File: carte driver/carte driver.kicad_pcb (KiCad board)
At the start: 2 copper layers, 120 x 50 mm, 76 parts, among them J1 UART CP, J10 STEPPER 4, J11 STEPPER 3, J2 Conn_01x03, J3 UART BONUS, J4 Conn_01x02, J6 STEPPER G, J7 STEPPER D, J8 STEPPER 1, J9 STEPPER 2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

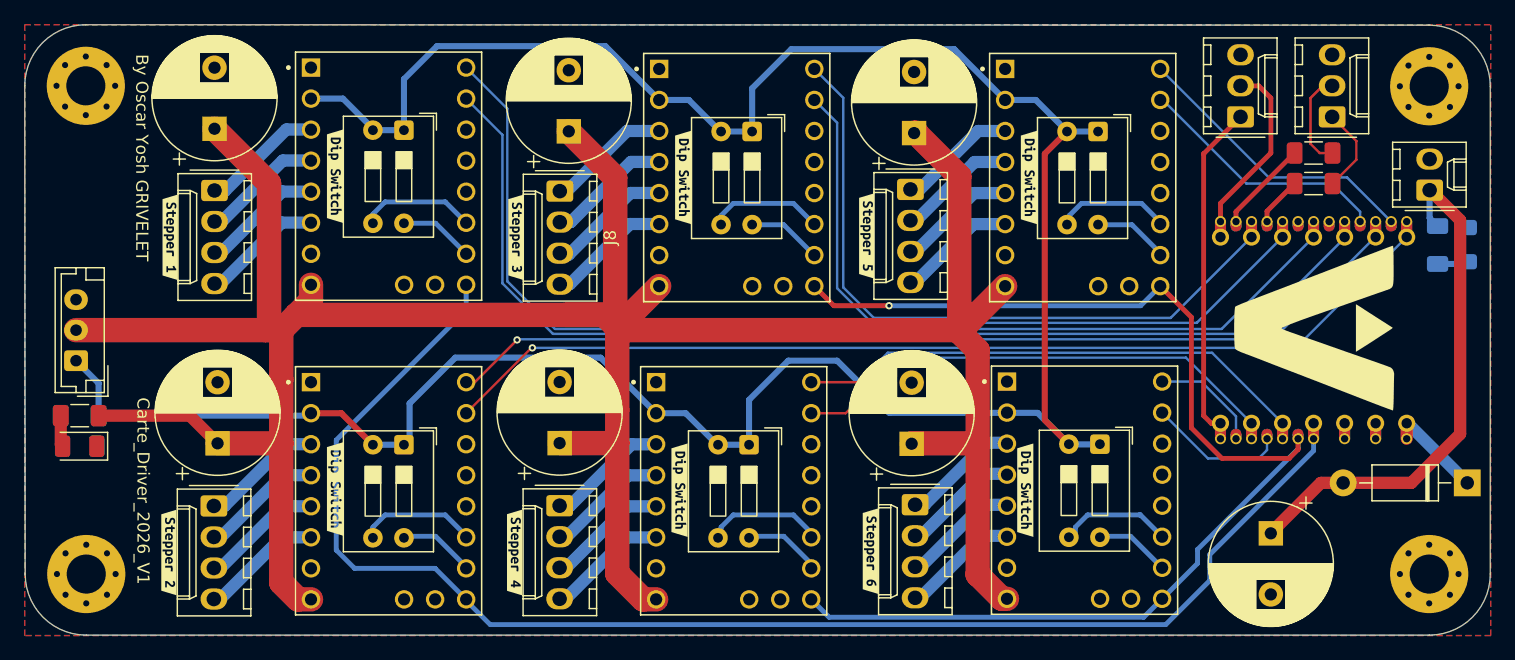
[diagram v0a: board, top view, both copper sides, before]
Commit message: changes power input and draw modif
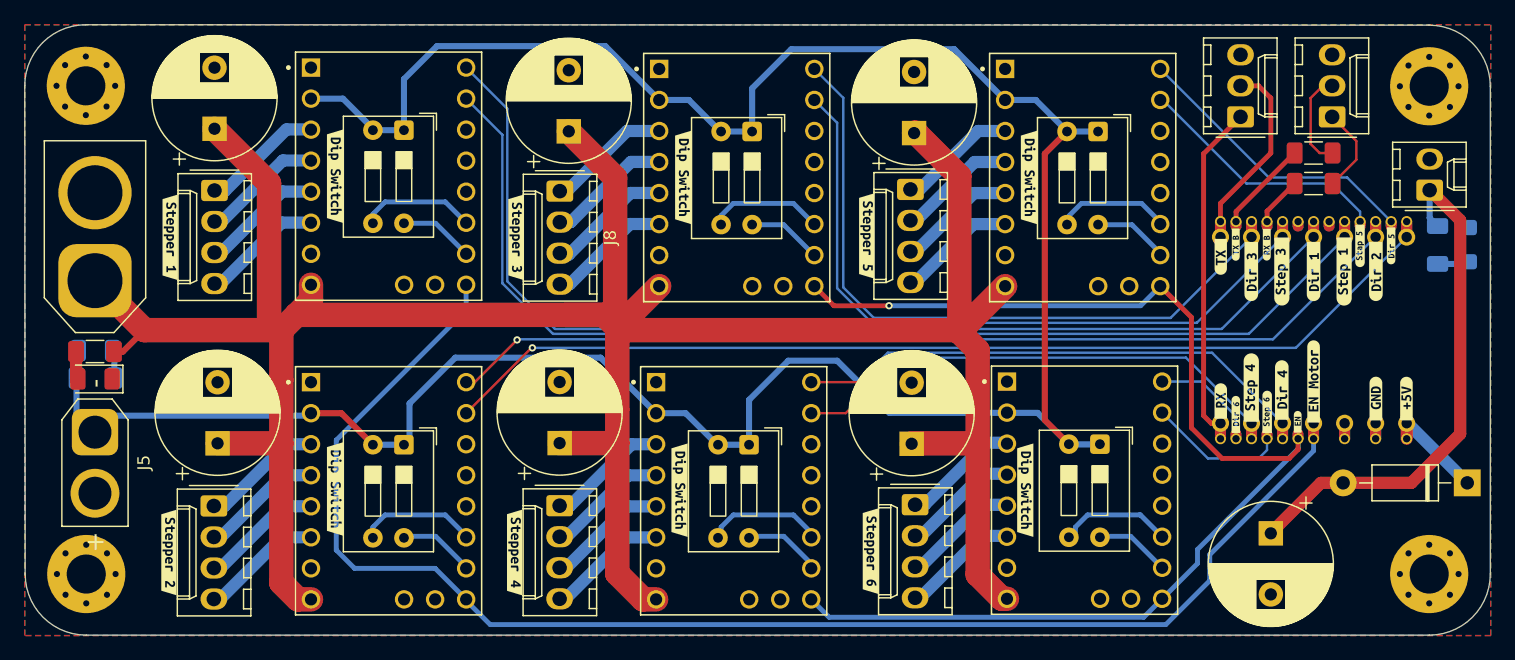
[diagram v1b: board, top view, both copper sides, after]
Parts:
- removed the G*** at (130.7, 150.0)
- removed J2: Conn_01x03, Connector_JST:JST_EH_B3B-EH-A_1x03_P2.50mm_Vertical
- removed the kibuzzard-68F7E6E6 at (126.7, 143.2)
- added J12: Conn_01x02, Connector_AMASS:AMASS_XT60-F_1x02_P7.20mm_Vertical, F.Cu at (30.8, 145.9)
- added J5: Conn_01x02, Connector_AMASS:AMASS_XT30U-F_1x02_P5.0mm_Vertical, F.Cu at (30.8, 158.3)
- added kibuzzard-690B42CF: G***, kibuzzard-690B42CF, F.Cu at (126.7, 143.0)
- added kibuzzard-690B42EC: G***, kibuzzard-690B42EC, F.Cu at (124.1, 143.0)
- kibuzzard-67ED8648, kibuzzard-68F7E57E, kibuzzard-68F7E5B2, kibuzzard-68F7E5C7, kibuzzard-68F7E5D0, kibuzzard-68F7E5E0, kibuzzard-68F7E5E6, kibuzzard-68F7E5EE, kibuzzard-68F7E6E6, kibuzzard-68F7E6FB, kibuzzard-68F7E70E, kibuzzard-68F7E71B, kibuzzard-68F7E74E, kibuzzard-68F7E766, kibuzzard-68F7E774, kibuzzard-68F7E782, kibuzzard-68F7E793: moved to F.Cu
- moved G*** 12.3 mm to (86.0, 151.5)
- moved D3 7.94 mm to (30.8, 151.7), turned to 0 degrees
- moved D4 5.64 mm to (30.8, 154.0)
- moved R4 5.40 mm to (30.8, 151.8)
- moved R3 3.34 mm to (30.8, 153.9), turned to 0 degrees
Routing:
- net +24V: track 239.0 -> 231.7 mm

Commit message: boh il y a des trucs à changé ducoup
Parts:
- moved J12 7.80 mm to (30.5, 138.2), turned to -90 degrees
- moved J5 4.91 mm to (30.5, 163.2), turned to 90 degrees
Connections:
- J12 pad 1: +24V -> GND
- J12 pad 2: GND -> +24V
- J5 pad 1: +3.3V -> GND
- J5 pad 2: GND -> +3.3V
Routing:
- net +3.3V: track 212.0 -> 213.8 mm
- net +24V: track 231.7 -> 232.4 mm

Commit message: deso alph
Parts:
- kibuzzard-68F7E5C0: moved to F.Cu
